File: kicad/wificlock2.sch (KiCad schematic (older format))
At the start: 3 parts, among them U1 DHT11, U1 ESP32-WROOM-32, U1 MAX7219

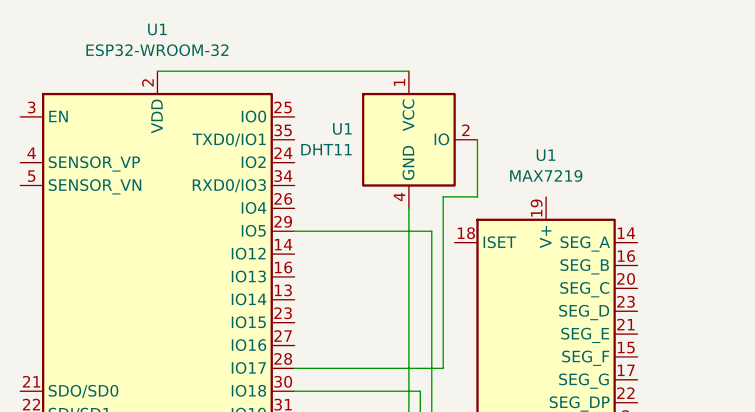
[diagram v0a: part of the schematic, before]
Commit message: Update kicad
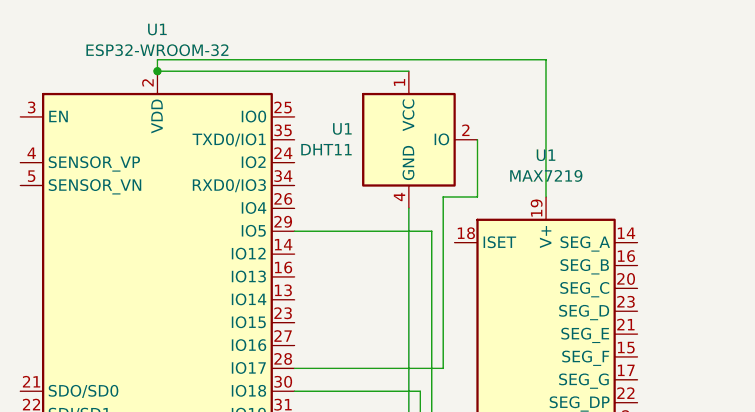
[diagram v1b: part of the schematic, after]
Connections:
- net at U1.1 (VCC), U1.2 (VDD): now also U1.19 (V+)
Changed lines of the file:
@@
 	1    0    0    -1
 $EndComp
+Wire Wire Line
+	6150 2600 6150 2550
+Wire Wire Line
+	6150 2550 7850 2550
+Wire Wire Line
+	7850 2550 7850 3150
+Connection ~ 6150 2600
 $EndSCHEMATC
